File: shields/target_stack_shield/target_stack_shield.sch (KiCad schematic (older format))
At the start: 12 parts, among them IC1 NCP1117DT33T5G, J1 GPIO shield connector 40pin, J2 probe shield connector 26pin, J3 PCIE-064-02-X-D-RA

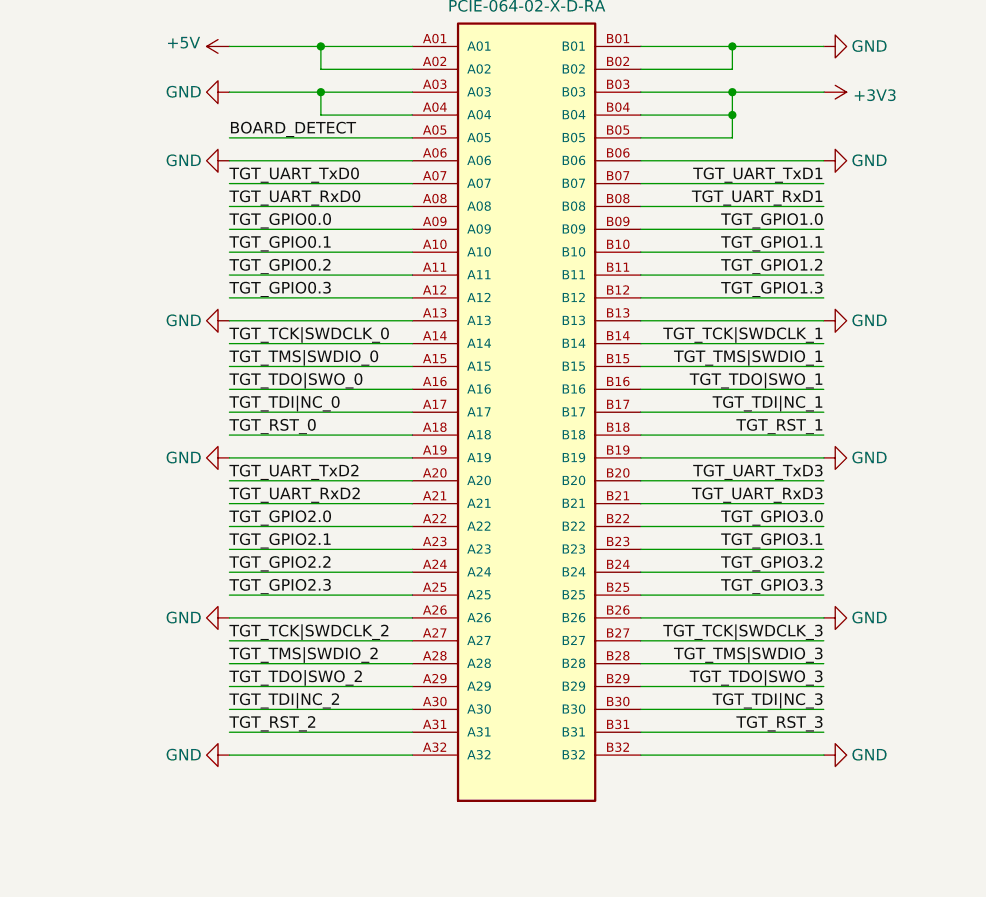
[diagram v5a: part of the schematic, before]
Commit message: finished target stack shield layout
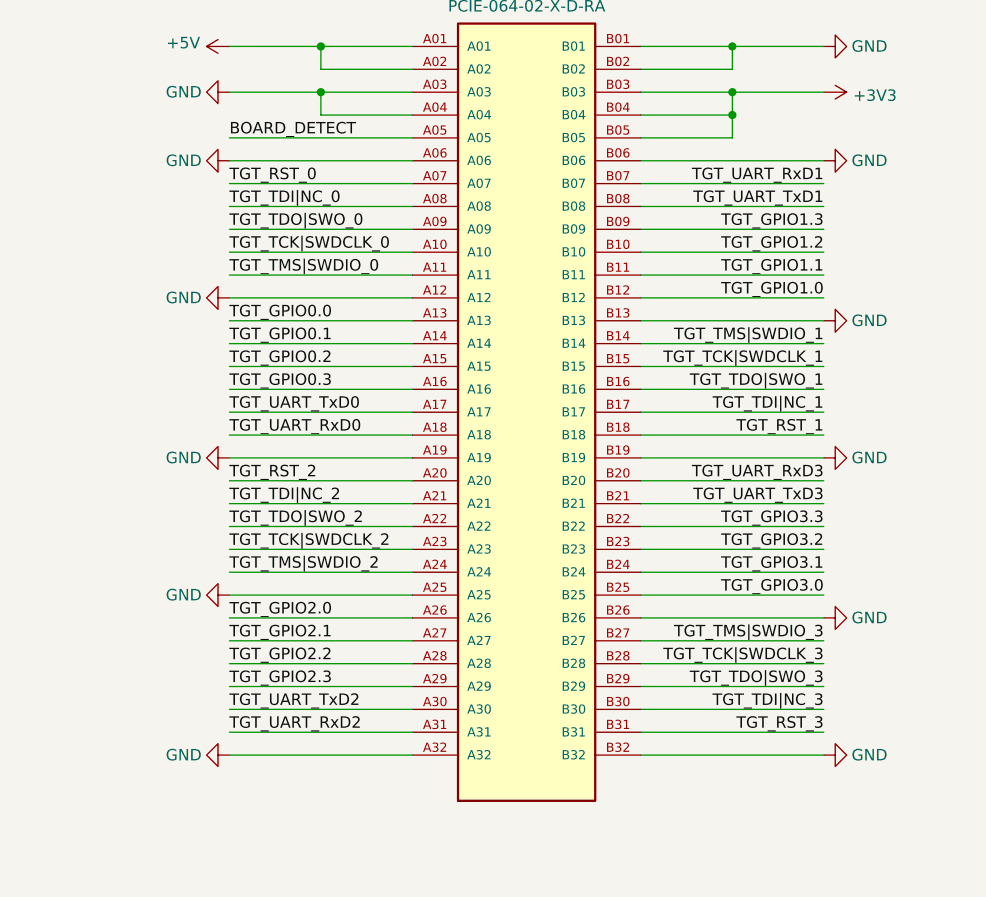
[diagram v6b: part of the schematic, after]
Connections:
- net GND: now also J3.A12, J3.A25; no longer J3.A13, J3.A26
- net TGT_GPIO0.0: now also J3.A13; no longer J3.A09
- net TGT_GPIO0.1: now also J3.A14; no longer J3.A10
- net TGT_GPIO0.2: now also J3.A15; no longer J3.A11
- net TGT_GPIO0.3: now also J3.A16; no longer J3.A12
- net TGT_GPIO1.0: now also J3.B12; no longer J3.B09
- net TGT_GPIO1.1: now also J3.B11; no longer J3.B10
- net TGT_GPIO1.2: now also J3.B10; no longer J3.B11
- net TGT_GPIO1.3: now also J3.B09; no longer J3.B12
- net TGT_GPIO2.0: now also J3.A26; no longer J3.A22
- net TGT_GPIO2.1: now also J3.A27; no longer J3.A23
- net TGT_GPIO2.2: now also J3.A28; no longer J3.A24
- net TGT_GPIO2.3: now also J3.A29; no longer J3.A25
- net TGT_GPIO3.0: now also J3.B25; no longer J3.B22
- net TGT_GPIO3.1: now also J3.B24; no longer J3.B23
- net TGT_GPIO3.2: now also J3.B23; no longer J3.B24
- net TGT_GPIO3.3: now also J3.B22; no longer J3.B25
- net TGT_RST_0: now also J3.A07; no longer J3.A18
- net TGT_RST_2: now also J3.A20; no longer J3.A31
- net TGT_TCK|SWDCLK_0: now also J3.A10; no longer J3.A14
- net TGT_TCK|SWDCLK_1: now also J3.B15; no longer J3.B14
- net TGT_TCK|SWDCLK_2: now also J3.A23; no longer J3.A27
- net TGT_TCK|SWDCLK_3: now also J3.B28; no longer J3.B27
- net TGT_TDI|NC_0: now also J3.A08; no longer J3.A17
- net TGT_TDI|NC_2: now also J3.A21; no longer J3.A30
- net TGT_TDO|SWO_0: now also J3.A09; no longer J3.A16
- net TGT_TDO|SWO_2: now also J3.A22; no longer J3.A29
- net TGT_TMS|SWDIO_0: now also J3.A11; no longer J3.A15
- net TGT_TMS|SWDIO_1: now also J3.B14; no longer J3.B15
- net TGT_TMS|SWDIO_2: now also J3.A24; no longer J3.A28
- net TGT_TMS|SWDIO_3: now also J3.B27; no longer J3.B28
- net TGT_UART_RxD0: now also J3.A18; no longer J3.A08
- net TGT_UART_RxD1: now also J3.B07; no longer J3.B08
- net TGT_UART_RxD2: now also J3.A31; no longer J3.A21
- net TGT_UART_RxD3: now also J3.B20; no longer J3.B21
- net TGT_UART_TxD0: now also J3.A17; no longer J3.A07
- net TGT_UART_TxD1: now also J3.B08; no longer J3.B07
- net TGT_UART_TxD2: now also J3.A30; no longer J3.A20
- net TGT_UART_TxD3: now also J3.B21; no longer J3.B20
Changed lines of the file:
@@
 Wire Wire Line
 	7450 2950 8250 2950
+Text Label 1950 4450 0    50   ~ 0
+TGT_TMS|SWDIO_0
+Text Label 1950 4350 0    50   ~ 0
+TGT_TCK|SWDCLK_0
+Text Label 1950 4250 0    50   ~ 0
+TGT_TDO|SWO_0
+Text Label 1950 4150 0    50   ~ 0
+TGT_TDI|NC_0
+Text Label 1950 4050 0    50   ~ 0
+TGT_RST_0
+Wire Wire Line
+	2750 4450 1950 4450
+Wire Wire Line
+	2750 4350 1950 4350
+Wire Wire Line
+	2750 4250 1950 4250
+Wire Wire Line
+	2750 4150 1950 4150
+Wire Wire Line
+	2750 4050 1950 4050
+Text Label 1950 4650 0    50   ~ 0
+TGT_GPIO0.0
+Wire Wire Line
+	1950 4650 2750 4650
+Text Label 1950 4750 0    50   ~ 0
+TGT_GPIO0.1
+Wire Wire Line
+	1950 4750 2750 4750
 Text Label 1950 4850 0    50   ~ 0
-TGT_TMS|SWDIO_0
-Text Label 1950 4750 0    50   ~ 0
-TGT_TCK|SWDCLK_0
+TGT_GPIO0.2
+Wire Wire Line
+	1950 4850 2750 4850
 Text Label 1950 4950 0    50   ~ 0
-TGT_TDO|SWO_0
-Text Label 1950 5050 0    50   ~ 0
-TGT_TDI|NC_0
-Text Label 1950 5150 0    50   ~ 0
-TGT_RST_0
-Wire Wire Line
-	2750 4850 1950 4850
-Wire Wire Line
-	2750 4750 1950 4750
-Wire Wire Line
-	2750 4950 1950 4950
-Wire Wire Line
-	2750 5050 1950 5050
-Wire Wire Line
-	2750 5150 1950 5150
-Text Label 1950 4250 0    50   ~ 0
-TGT_GPIO0.0
-Wire Wire Line
-	1950 4250 2750 4250
-Text Label 1950 4350 0    50   ~ 0
-TGT_GPIO0.1
-Wire Wire Line
-	1950 4350 2750 4350
-Text Label 1950 4450 0    50   ~ 0
-TGT_GPIO0.2
-Wire Wire Line
-	1950 4450 2750 4450
-Text Label 1950 4550 0    50   ~ 0
 TGT_GPIO0.3
 Wire Wire Line
-	1950 4550 2750 4550
-Text Label 1950 4050 0    50   ~ 0
-TGT_UART_TxD0
-Wire Wire Line
-	1950 4050 2750 4050
-Text Label 1950 4150 0    50   ~ 0
-TGT_UART_RxD0
+	1950 4950 2750 4950
 Wire Wire Line
 	1950 3850 2750 3850
@@
 $EndComp
 Wire Wire Line
-	1950 5950 2750 5950
+	1950 5850 2750 5850
 $Comp
 L power:GND #PWR07
 U 1 1 61CCE621
-P 1950 5950
-F 0 "#PWR07" H 1950 5700 50  0001 C CNN
-F 1 "GND" V 1950 5750 50  0000 C CNN
-F 2 "" H 1950 5950 50  0001 C CNN
-F 3 "" H 1950 5950 50  0001 C CNN
-	1    1950 5950
+P 1950 5850
+F 0 "#PWR07" H 1950 5600 50  0001 C CNN
+F 1 "GND" V 1950 5650 50  0000 C CNN
+F 2 "" H 1950 5850 50  0001 C CNN
+F 3 "" H 1950 5850 50  0001 C CNN
+	1    1950 5850
 	0    1    1    0
 $EndComp
@@
 $EndComp
 Wire Wire Line
-	1950 4650 2750 4650
+	1950 4550 2750 4550
 $Comp
 L power:GND #PWR05
 U 1 1 61D03625
-P 1950 4650
-F 0 "#PWR05" H 1950 4400 50  0001 C CNN
-F 1 "GND" V 1950 4450 50  0000 C CNN
-F 2 "" H 1950 4650 50  0001 C CNN
-F 3 "" H 1950 4650 50  0001 C CNN
-	1    1950 4650
+P 1950 4550
+F 0 "#PWR05" H 1950 4300 50  0001 C CNN
+F 1 "GND" V 1950 4350 50  0000 C CNN
+F 2 "" H 1950 4550 50  0001 C CNN
+F 3 "" H 1950 4550 50  0001 C CNN
+	1    1950 4550
 	0    1    1    0
 $EndComp
@@
 Text Label 1950 3850 0    50   ~ 0
 BOARD_DETECT
-Wire Wire Line
-	1950 4150 2750 4150
+Text Label 1950 5750 0    50   ~ 0
+TGT_TMS|SWDIO_2
+Text Label 1950 5650 0    50   ~ 0
+TGT_TCK|SWDCLK_2
+Text Label 1950 5550 0    50   ~ 0
+TGT_TDO|SWO_2
+Text Label 1950 5450 0    50   ~ 0
+TGT_TDI|NC_2
+Text Label 1950 5350 0    50   ~ 0
+TGT_RST_2
+Wire Wire Line
+	2750 5750 1950 5750
+Wire Wire Line
+	2750 5650 1950 5650
+Wire Wire Line
+	2750 5550 1950 5550
+Wire Wire Line
+	2750 5450 1950 5450
+Wire Wire Line
+	2750 5350 1950 5350
+Text Label 1950 5950 0    50   ~ 0
+TGT_GPIO2.0
+Wire Wire Line
+	1950 5950 2750 5950
+Text Label 1950 6050 0    50   ~ 0
+TGT_GPIO2.1
+Wire Wire Line
+	1950 6050 2750 6050
 Text Label 1950 6150 0    50   ~ 0
-TGT_TMS|SWDIO_2
-Text Label 1950 6050 0    50   ~ 0
-TGT_TCK|SWDCLK_2
+TGT_GPIO2.2
+Wire Wire Line
+	1950 6150 2750 6150
 Text Label 1950 6250 0    50   ~ 0
-TGT_TDO|SWO_2
+TGT_GPIO2.3
+Wire Wire Line
+	1950 6250 2750 6250
 Text Label 1950 6350 0    50   ~ 0
-TGT_TDI|NC_2
+TGT_UART_TxD2
+Wire Wire Line
+	1950 6350 2750 6350
 Text Label 1950 6450 0    50   ~ 0
-TGT_RST_2
-Wire Wire Line
-	2750 6150 1950 6150
-Wire Wire Line
-	2750 6050 1950 6050
-Wire Wire Line
-	2750 6250 1950 6250
-Wire Wire Line
-	2750 6350 1950 6350
-Wire Wire Line
-	2750 6450 1950 6450
-Text Label 1950 5550 0    50   ~ 0
-TGT_GPIO2.0
-Wire Wire Line
-	1950 5550 2750 5550
-Text Label 1950 5650 0    50   ~ 0
-TGT_GPIO2.1
-Wire Wire Line
-	1950 5650 2750 5650
-Text Label 1950 5750 0    50   ~ 0
-TGT_GPIO2.2
-Wire Wire Line
-	1950 5750 2750 5750
-Text Label 1950 5850 0    50   ~ 0
-TGT_GPIO2.3
-Wire Wire Line
-	1950 5850 2750 5850
-Text Label 1950 5350 0    50   ~ 0
-TGT_UART_TxD2
-Wire Wire Line
-	1950 5350 2750 5350
-Text Label 1950 5450 0    50   ~ 0
 TGT_UART_RxD2
 Wire Wire Line
-	1950 5450 2750 5450
+	1950 6450 2750 6450
 Text Notes 8500 1350 0    99   ~ 0
 Bus Switches
@@
 Wire Wire Line
 	7450 4150 8250 4150
+Text Label 4550 4750 2    50   ~ 0
+TGT_TMS|SWDIO_1
 Text Label 4550 4850 2    50   ~ 0
-TGT_TMS|SWDIO_1
-Text Label 4550 4750 2    50   ~ 0
 TGT_TCK|SWDCLK_1
 Text Label 4550 4950 2    50   ~ 0
@@
 TGT_RST_1
 Wire Wire Line
+	3750 4750 4550 4750
+Wire Wire Line
 	3750 4850 4550 4850
 Wire Wire Line
-	3750 4750 4550 4750
-Wire Wire Line
 	3750 4950 4550 4950
 Wire Wire Line
@@
 Wire Wire Line
 	3750 5150 4550 5150
+Text Label 4550 4550 2    50   ~ 0
+TGT_GPIO1.0
+Wire Wire Line
+	4550 4550 3750 4550
+Text Label 4550 4450 2    50   ~ 0
+TGT_GPIO1.1
+Wire Wire Line
+	4550 4450 3750 4450
+Text Label 4550 4350 2    50   ~ 0
+TGT_GPIO1.2
+Wire Wire Line
+	4550 4350 3750 4350
 Text Label 4550 4250 2    50   ~ 0
-TGT_GPIO1.0
+TGT_GPIO1.3
 Wire Wire Line
 	4550 4250 3750 4250
-Text Label 4550 4350 2    50   ~ 0
-TGT_GPIO1.1
-Wire Wire Line
-	4550 4350 3750 4350
-Text Label 4550 4450 2    50   ~ 0
-TGT_GPIO1.2
-Wire Wire Line
-	4550 4450 3750 4450
-Text Label 4550 4550 2    50   ~ 0
-TGT_GPIO1.3
-Wire Wire Line
-	4550 4550 3750 4550
+Text Label 4550 4150 2    50   ~ 0
+TGT_UART_TxD1
+Wire Wire Line
+	4550 4150 3750 4150
 Text Label 4550 4050 2    50   ~ 0
-TGT_UART_TxD1
+TGT_UART_RxD1
 Wire Wire Line
 	4550 4050 3750 4050
-Text Label 4550 4150 2    50   ~ 0
-TGT_UART_RxD1
-Wire Wire Line
-	4550 4150 3750 4150
+Text Label 4550 6050 2    50   ~ 0
+TGT_TMS|SWDIO_3
 Text Label 4550 6150 2    50   ~ 0
-TGT_TMS|SWDIO_3
-Text Label 4550 6050 2    50   ~ 0
 TGT_TCK|SWDCLK_3
 Text Label 4550 6250 2    50   ~ 0
@@
 TGT_RST_3
 Wire Wire Line
+	3750 6050 4550 6050
+Wire Wire Line
 	3750 6150 4550 6150
 Wire Wire Line
-	3750 6050 4550 6050
-Wire Wire Line
 	3750 6250 4550 6250
 Wire Wire Line
@@
 	3750 6450 4550 6450
 Wire Wire Line
+	4550 5850 3750 5850
+Text Label 4550 5750 2    50   ~ 0
+TGT_GPIO3.1
+Wire Wire Line
+	4550 5750 3750 5750
+Text Label 4550 5650 2    50   ~ 0
+TGT_GPIO3.2
+Wire Wire Line
+	4550 5650 3750 5650
+Text Label 4550 5550 2    50   ~ 0
+TGT_GPIO3.3
+Wire Wire Line
 	4550 5550 3750 5550
-Text Label 4550 5650 2    50   ~ 0
-TGT_GPIO3.1
-Wire Wire Line
-	4550 5650 3750 5650
-Text Label 4550 5750 2    50   ~ 0
-TGT_GPIO3.2
-Wire Wire Line
-	4550 5750 3750 5750
+Text Label 4550 5450 2    50   ~ 0
+TGT_UART_TxD3
+Wire Wire Line
+	4550 5450 3750 5450
+Text Label 4550 5350 2    50   ~ 0
+TGT_UART_RxD3
+Wire Wire Line
+	4550 5350 3750 5350
 Text Label 4550 5850 2    50   ~ 0
-TGT_GPIO3.3
-Wire Wire Line
-	4550 5850 3750 5850
-Text Label 4550 5350 2    50   ~ 0
-TGT_UART_TxD3
-Wire Wire Line
-	4550 5350 3750 5350
-Text Label 4550 5450 2    50   ~ 0
-TGT_UART_RxD3
-Wire Wire Line
-	4550 5450 3750 5450
-Text Label 4550 5550 2    50   ~ 0
 TGT_GPIO3.0
 Wire Wire Line
@@
 Wire Wire Line
 	900  1600 900  1400
+Wire Wire Line
+	1950 5150 2750 5150
+Text Label 1950 5150 0    50   ~ 0
+TGT_UART_RxD0
+Wire Wire Line
+	1950 5050 2750 5050
+Text Label 1950 5050 0    50   ~ 0
+TGT_UART_TxD0
 $EndSCHEMATC

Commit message: added partlist and prices
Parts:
- C1, C2: Digikey Price (CHF) (none) -> 0.15; Manufacturer_Part_Number (none) -> LMK212ABJ106MG-T; Mouser Price (CHF) (none) -> 0.13
- H1, H2, H3, H4, R1: Digikey Price (CHF) (none) -> -; Mouser Price (CHF) (none) -> -
- IC1: Digikey Price (CHF) (none) -> 0.62; Mouser Price (CHF) (none) -> 0.64
- J1: Digikey Price (CHF) (none) -> 2.74; Manufacturer_Part_Number (none) -> Adafruit 1979; Mouser Price (CHF) (none) -> 2.77
- J2: Digikey Price (CHF) (none) -> 1.81; Manufacturer_Part_Number (none) -> Adafruit 1112; Mouser Price (CHF) (none) -> 1.82
- J3: Digikey Price (CHF) (none) -> 5.46; Manufacturer_Part_Number (none) -> PCIE-064-02-F-D-RA; Mouser Price (CHF) (none) -> 5.17
- LED1: Digikey Price (CHF) (none) -> 0.14; Mouser Price (CHF) (none) -> 0.13
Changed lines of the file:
@@
 F 7 "ON Semiconductor" H 5000 850 50  0001 L CNN "Manufacturer_Name"
 F 8 "NCP1117DT33T5G" H 5000 750 50  0001 L CNN "Manufacturer_Part_Number"
+F 9 "0.62" H 3650 1350 50  0001 C CNN "Digikey Price (CHF)"
+F 10 "0.64" H 3650 1350 50  0001 C CNN "Mouser Price (CHF)"
 	1    3650 1350
 	1    0    0    -1
@@
 F 2 "Capacitor_SMD:C_0805_2012Metric_Pad1.15x1.40mm_HandSolder" H 3300 1450 50  0001 C CNN
 F 3 "~" H 3300 1450 50  0001 C CNN
+F 4 "0.15" H 3300 1450 50  0001 C CNN "Digikey Price (CHF)"
+F 5 "LMK212ABJ106MG-T" H 3300 1450 50  0001 C CNN "Manufacturer_Part_Number"
+F 6 "0.13" H 3300 1450 50  0001 C CNN "Mouser Price (CHF)"
 	1    3300 1450
 	1    0    0    -1
@@
 F 2 "Capacitor_SMD:C_0805_2012Metric_Pad1.15x1.40mm_HandSolder" H 5400 1450 50  0001 C CNN
 F 3 "~" H 5400 1450 50  0001 C CNN
+F 4 "0.15" H 5400 1450 50  0001 C CNN "Digikey Price (CHF)"
+F 5 "LMK212ABJ106MG-T" H 5400 1450 50  0001 C CNN "Manufacturer_Part_Number"
+F 6 "0.13" H 5400 1450 50  0001 C CNN "Mouser Price (CHF)"
 	1    5400 1450
 	1    0    0    -1
@@
 F 2 "Resistor_SMD:R_0603_1608Metric_Pad1.05x0.95mm_HandSolder" H 6000 1600 50  0001 C CNN
 F 3 "~" H 6000 1600 50  0001 C CNN
+F 4 "-" H 6000 1600 50  0001 C CNN "Digikey Price (CHF)"
+F 5 "-" H 6000 1600 50  0001 C CNN "Mouser Price (CHF)"
 	1    6000 1600
 	1    0    0    -1
@@
 F 8 "Wurth Elektronik" H 6500 1850 50  0001 L BNN "Manufacturer_Name"
 F 9 "150060VS75000" H 6500 1750 50  0001 L BNN "Manufacturer_Part_Number"
+F 10 "0.14" H 6000 2300 50  0001 C CNN "Digikey Price (CHF)"
+F 11 "0.13" H 6000 2300 50  0001 C CNN "Mouser Price (CHF)"
 	1    6000 2300
 	0    -1   -1   0
@@
 F 2 "hive:PinHeader_2x20_P2.54mm_Vertical_gpio_shield" H 13500 2700 50  0001 C CNN
 F 3 "~" H 13500 2700 50  0001 C CNN
+F 4 "Adafruit 1979" H 13500 2700 50  0001 C CNN "Manufacturer_Part_Number"
+F 5 "2.77" H 13500 2700 50  0001 C CNN "Mouser Price (CHF)"
+F 6 "2.74" H 13500 2700 50  0001 C CNN "Digikey Price (CHF)"
 	1    13500 2700
 	1    0    0    -1
@@
 F 2 "hive:PinHeader_2x13_P2.54mm_Vertical_probe_shield" H 13500 5400 50  0001 C CNN
 F 3 "~" H 13500 5400 50  0001 C CNN
+F 4 "1.81" H 13500 5400 50  0001 C CNN "Digikey Price (CHF)"
+F 5 "Adafruit 1112" H 13500 5400 50  0001 C CNN "Manufacturer_Part_Number"
+F 6 "1.82" H 13500 5400 50  0001 C CNN "Mouser Price (CHF)"
 	1    13500 5400
 	1    0    0    -1
@@
 F 6 "D" H 3250 5050 50  0001 L BNN "PARTREV"
 F 7 "9.58mm" H 3250 5050 50  0001 L BNN "MAXIMUM_PACKAGE_HEIGHT"
+F 8 "5.46" H 3250 5050 50  0001 C CNN "Digikey Price (CHF)"
+F 9 "PCIE-064-02-F-D-RA" H 3250 5050 50  0001 C CNN "Manufacturer_Part_Number"
+F 10 "5.17" H 3250 5050 50  0001 C CNN "Mouser Price (CHF)"
 	1    3250 5050
 	1    0    0    -1
@@
 F 2 "MountingHole:MountingHole_2.7mm_M2.5_DIN965_Pad" H 1150 1000 50  0001 C CNN
 F 3 "~" H 1150 1000 50  0001 C CNN
+F 4 "-" H 1150 1000 50  0001 C CNN "Digikey Price (CHF)"
+F 5 "-" H 1150 1000 50  0001 C CNN "Mouser Price (CHF)"
 	1    1150 1000
 	0    1    1    0
@@
 F 2 "MountingHole:MountingHole_2.7mm_M2.5_DIN965_Pad" H 1150 1200 50  0001 C CNN
 F 3 "~" H 1150 1200 50  0001 C CNN
+F 4 "-" H 1150 1200 50  0001 C CNN "Digikey Price (CHF)"
+F 5 "-" H 1150 1200 50  0001 C CNN "Mouser Price (CHF)"
 	1    1150 1200
 	0    1    1    0
@@
 F 2 "MountingHole:MountingHole_2.7mm_M2.5_DIN965_Pad" H 1150 1400 50  0001 C CNN
 F 3 "~" H 1150 1400 50  0001 C CNN
+F 4 "-" H 1150 1400 50  0001 C CNN "Digikey Price (CHF)"
+F 5 "-" H 1150 1400 50  0001 C CNN "Mouser Price (CHF)"
 	1    1150 1400
 	0    1    1    0
@@
 F 2 "MountingHole:MountingHole_2.7mm_M2.5_DIN965_Pad" H 1150 1600 50  0001 C CNN
 F 3 "~" H 1150 1600 50  0001 C CNN
+F 4 "-" H 1150 1600 50  0001 C CNN "Digikey Price (CHF)"
+F 5 "-" H 1150 1600 50  0001 C CNN "Mouser Price (CHF)"
 	1    1150 1600
 	0    1    1    0
